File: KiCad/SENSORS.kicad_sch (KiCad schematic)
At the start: 10 parts, among them IC1 A3144EUA, J25 Screw_Terminal_01x02, U1 TMP102xxDRL

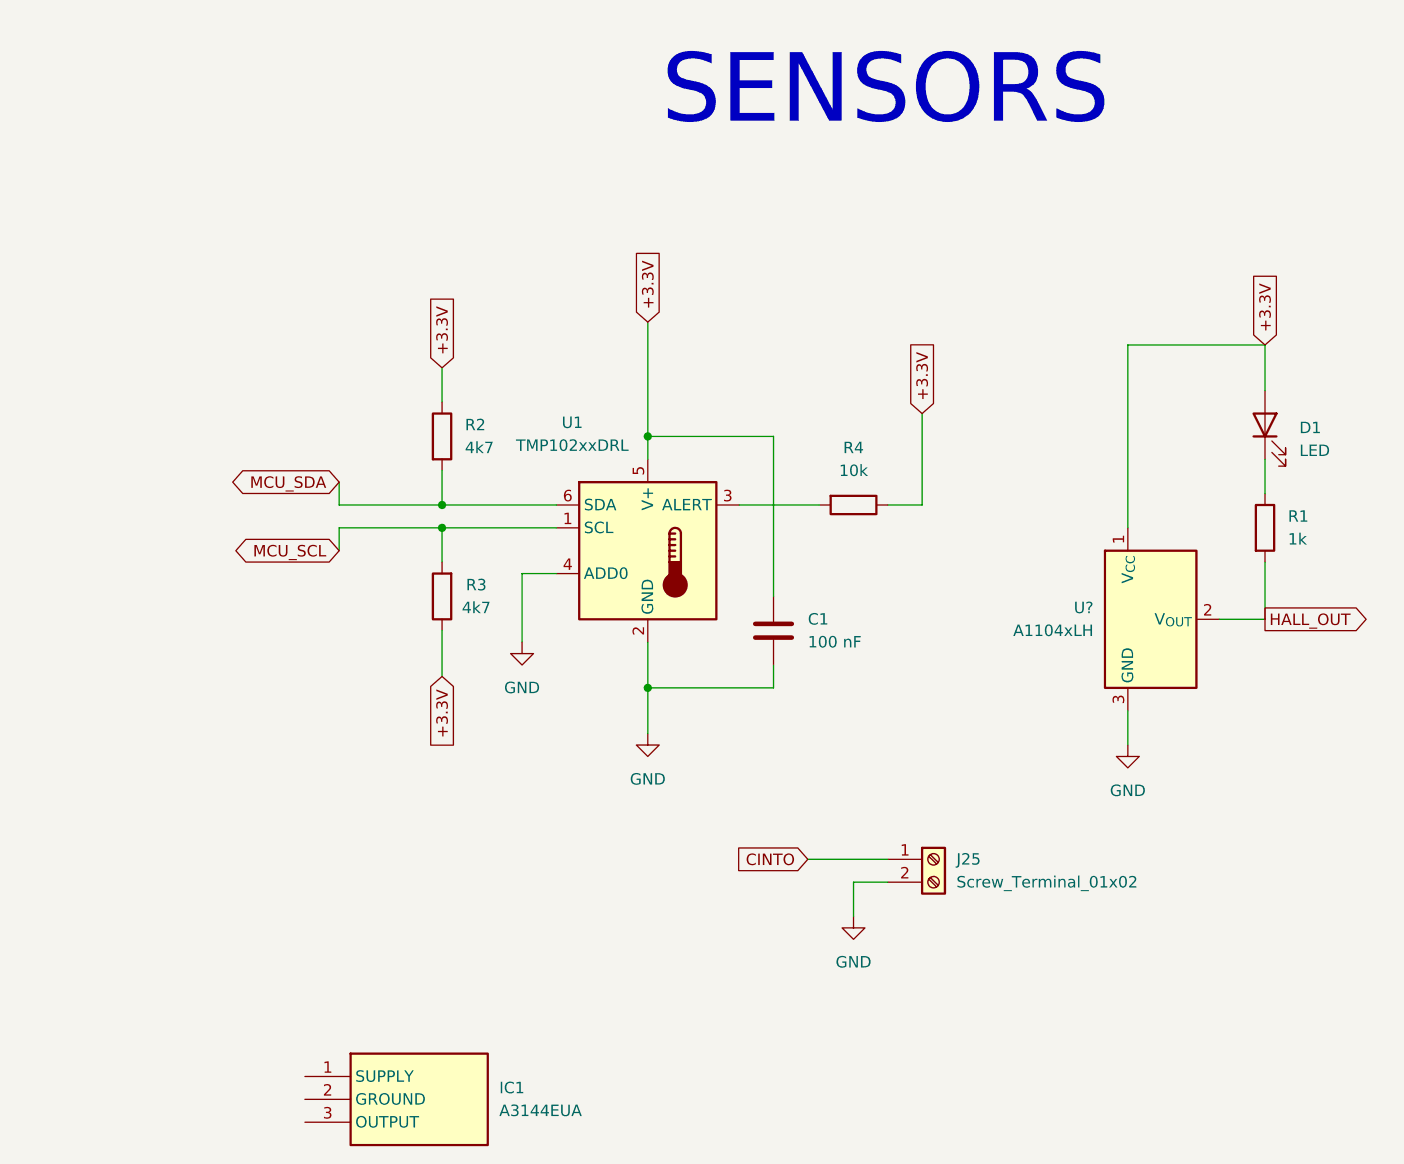
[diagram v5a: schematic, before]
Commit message: Modificació al HALL A3144
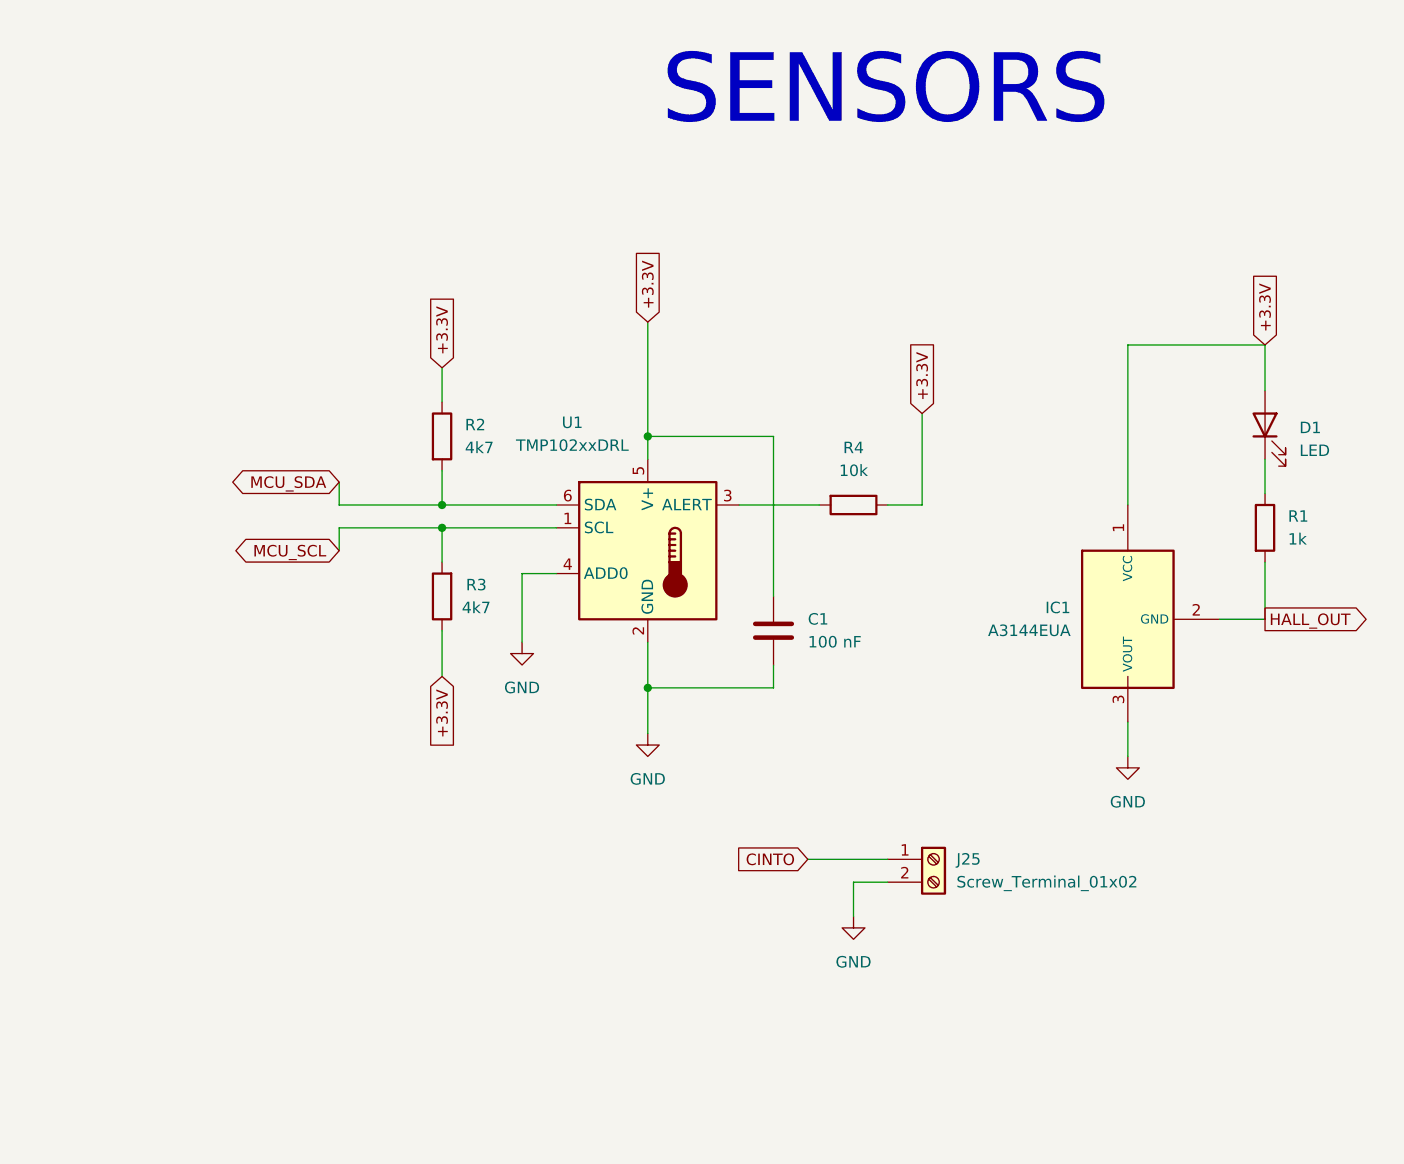
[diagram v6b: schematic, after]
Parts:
- removed U?: A1104xLH, Package_TO_SOT_SMD:SOT-23W, symbol Sensor_Magnetic:A1104xLH
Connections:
- net +3.3V: now also IC1.1 (VCC)
- net GND: now also IC1.3 (VOUT)
- net HALL_OUT: now also IC1.2 (GND)
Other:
- moved on the sheet: IC1
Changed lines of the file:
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@@
 	(wire
 		(pts
-			(xy 176.53 124.46) (xy 176.53 128.27)
+			(xy 176.53 125.73) (xy 176.53 129.54)
 		)
 		(stroke
@@
 	(wire
 		(pts
-			(xy 176.53 104.14) (xy 176.53 83.82)
+			(xy 176.53 101.6) (xy 176.53 83.82)
 		)
 		(stroke
@@
 	)
 	(symbol
-		(lib_name "A1104xLH_1")
-		(lib_id "Sensor_Magnetic:A1104xLH")
-		(at 179.07 114.3 0)
+		(lib_id "A3144:A3144EUA")
+		(at 166.37 110.49 0)
 		(unit 1)
 		(exclude_from_sim no)
@@
 		(dnp no)
 		(fields_autoplaced yes)
-		(property "Reference" "U?"
-			(at 172.72 113.0299 0)
+		(property "Reference" "IC1"
+			(at 170.18 113.0299 0)
 			(effects
 				(font
@@
 			)
 		)
-		(property "Value" "A1104xLH"
-			(at 172.72 115.5699 0)
+		(property "Value" "A3144EUA"
+			(at 170.18 115.5699 0)
 			(effects
 				(font
@@
 			)
 		)
-		(property "Footprint" "Package_TO_SOT_SMD:SOT-23W"
-			(at 179.07 131.572 0)
-			(effects
-				(font
-					(size 1.27 1.27)
-					(italic yes)
-				)
-				(hide yes)
-			)
-		)
-		(property "Datasheet" "https://www.allegromicro.com/-/media/files/datasheets/a110x-datasheet.ashx"
-			(at 179.07 127 0)
-			(effects
-				(font
-					(size 1.27 1.27)
-				)
-				(hide yes)
-			)
-		)
-		(property "Description" "Hall effect switch, unipolar (south-polarity), Bop=70-350G, Brp=50-330G, 3.8-24V supply, SOT-23W"
-			(at 179.07 129.286 0)
-			(effects
-				(font
-					(size 1.27 1.27)
-				)
-				(hide yes)
-			)
-		)
-		(pin "3"
-		)
-		(pin "2"
-		)
-		(pin "1"
-		)
-		(instances
-			(project "SENSORS"
-				(path "/264905d4-7c45-4183-babb-a5b2177ba886"
-					(reference "U?")
-					(unit 1)
-				)
-			)
-			(project ""
-				(path "/b6401b4f-5426-49b8-bb2e-8ecdb19989ef/e4bd2572-b2cc-4f8d-9ea8-3fa488d49274"
-					(reference "U9")
-					(unit 1)
-				)
-			)
-		)
-	)
-	(symbol
-		(lib_id "A3144:A3144EUA")
-		(at 85.09 165.1 0)
-		(unit 1)
-		(exclude_from_sim no)
-		(in_bom yes)
-		(on_board yes)
-		(dnp no)
-		(fields_autoplaced yes)
-		(property "Reference" "IC1"
-			(at 106.68 166.3699 0)
-			(effects
-				(font
-					(size 1.27 1.27)
-				)
-				(justify left)
-			)
-		)
-		(property "Value" "A3144EUA"
-			(at 106.68 168.9099 0)
-			(effects
-				(font
-					(size 1.27 1.27)
-				)
-				(justify left)
-			)
-		)
 		(property "Footprint" "A3144:A3144EUA"
-			(at 106.68 260.02 0)
+			(at 187.96 205.41 0)
 			(effects
 				(font
@@
 		)
 		(property "Datasheet" "https://pdf1.alldatasheet.com/datasheet-pdf/download/90853/ALLEGRO/A3144EUA.html"
-			(at 106.68 360.02 0)
+			(at 187.96 305.41 0)
 			(effects
 				(font
@@
 		)
 		(property "Description" "SENSITIVE HALL-EFFECT SWITCHES FOR HIGH-TEMPERATURE OPERATION"
-			(at 85.09 165.1 0)
+			(at 166.37 110.49 0)
 			(effects
 				(font
@@
 		)
 		(property "Height" "5.26"
-			(at 106.68 560.02 0)
+			(at 187.96 505.41 0)
 			(effects
 				(font
@@
 		)
 		(property "Manufacturer_Name" "Allegro Microsystems"
-			(at 106.68 660.02 0)
+			(at 187.96 605.41 0)
 			(effects
 				(font
@@
 		)
 		(property "Manufacturer_Part_Number" "A3144EUA"
-			(at 106.68 760.02 0)
+			(at 187.96 705.41 0)
 			(effects
 				(font
@@
 		)
 		(property "Mouser Part Number" ""
-			(at 106.68 860.02 0)
+			(at 187.96 805.41 0)
 			(effects
 				(font
@@
 		)
 		(property "Mouser Price/Stock" ""
-			(at 106.68 960.02 0)
+			(at 187.96 905.41 0)
 			(effects
 				(font
@@
 		)
 		(property "Arrow Part Number" ""
-			(at 106.68 1060.02 0)
+			(at 187.96 1005.41 0)
 			(effects
 				(font
@@
 		)
 		(property "Arrow Price/Stock" ""
-			(at 106.68 1160.02 0)
+			(at 187.96 1105.41 0)
 			(effects
 				(font
@@
 	(symbol
 		(lib_id "power:GND")
-		(at 176.53 128.27 0)
+		(at 176.53 129.54 0)
 		(unit 1)
 		(exclude_from_sim no)
@@
 		(fields_autoplaced yes)
 		(property "Reference" "#PWR03"
+			(at 176.53 135.89 0)
+			(effects
+				(font
+					(size 1.27 1.27)
+				)
+				(hide yes)
+			)
+		)
+		(property "Value" "GND"
 			(at 176.53 134.62 0)
 			(effects
@@
 					(size 1.27 1.27)
 				)
-				(hide yes)
-			)
-		)
-		(property "Value" "GND"
-			(at 176.53 133.35 0)
-			(effects
-				(font
-					(size 1.27 1.27)
-				)
 			)
 		)
 		(property "Footprint" ""
-			(at 176.53 128.27 0)
+			(at 176.53 129.54 0)
 			(effects
 				(font
@@
 		)
 		(property "Datasheet" ""
-			(at 176.53 128.27 0)
+			(at 176.53 129.54 0)
 			(effects
 				(font
@@
 		)
 		(property "Description" "Power symbol creates a global label with name \"GND\" , ground"
-			(at 176.53 128.27 0)
-			(effects
-				(font
+			(at 176.53 129.54 0)
+			(effects
+				(font

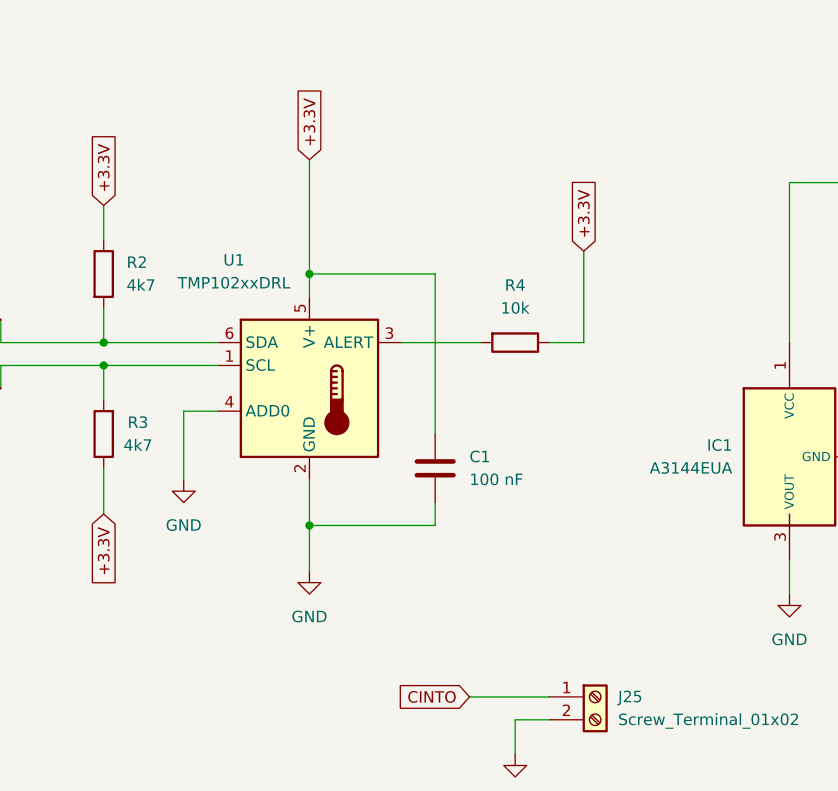
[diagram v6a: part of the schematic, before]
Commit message: Modificació als SENSORS
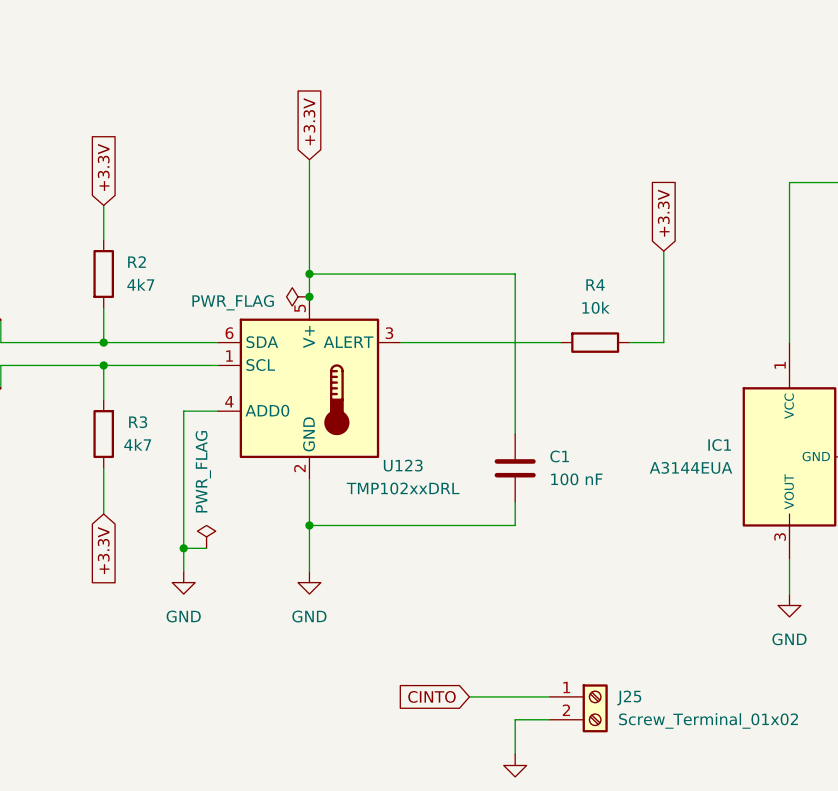
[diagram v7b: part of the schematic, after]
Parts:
- renumbered U1 to U123
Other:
- moved on the sheet: C1, R4
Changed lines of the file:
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@@
+	)
+	(junction
+		(at 109.22 124.46)
+		(diameter 0)
+		(color 0 0 0 0)
 	)
 	(junction
@@
 		(color 0 0 0 0)
 	)
+	(junction
+		(at 123.19 96.52)
+		(diameter 0)
+		(color 0 0 0 0)
+	)
 	(wire
 		(pts
@@
 	(wire
 		(pts
-			(xy 153.67 101.6) (xy 153.67 91.44)
+			(xy 162.56 101.6) (xy 162.56 91.44)
 		)
 		(stroke
@@
 	(wire
 		(pts
+			(xy 109.22 124.46) (xy 111.76 124.46)
+		)
+		(stroke
+			(width 0)
+			(type default)
+		)
+	)
+	(wire
+		(pts
 			(xy 88.9 104.14) (xy 88.9 106.68)
 		)
@@
 	(wire
 		(pts
-			(xy 137.16 93.98) (xy 123.19 93.98)
-		)
-		(stroke
-			(width 0)
-			(type default)
-		)
-	)
-	(wire
-		(pts
 			(xy 191.77 96.52) (xy 191.77 100.33)
 		)
@@
 	(wire
 		(pts
-			(xy 137.16 121.92) (xy 123.19 121.92)
+			(xy 123.19 121.92) (xy 146.05 121.92)
 		)
 		(stroke
@@
 	(wire
 		(pts
-			(xy 149.86 101.6) (xy 153.67 101.6)
+			(xy 158.75 101.6) (xy 162.56 101.6)
+		)
+		(stroke
+			(width 0)
+			(type default)
+		)
+	)
+	(wire
+		(pts
+			(xy 133.35 101.6) (xy 151.13 101.6)
 		)
 		(stroke
@@
 	(wire
 		(pts
-			(xy 133.35 101.6) (xy 142.24 101.6)
-		)
-		(stroke
-			(width 0)
-			(type default)
-		)
-	)
-	(wire
-		(pts
-			(xy 137.16 111.76) (xy 137.16 93.98)
-		)
-		(stroke
-			(width 0)
-			(type default)
-		)
-	)
-	(wire
-		(pts
-			(xy 109.22 109.22) (xy 109.22 116.84)
+			(xy 146.05 111.76) (xy 146.05 93.98)
+		)
+		(stroke
+			(width 0)
+			(type default)
+		)
+	)
+	(wire
+		(pts
+			(xy 123.19 93.98) (xy 146.05 93.98)
+		)
+		(stroke
+			(width 0)
+			(type default)
+		)
+	)
+	(wire
+		(pts
+			(xy 109.22 109.22) (xy 109.22 124.46)
 		)
 		(stroke
@@
 	(wire
 		(pts
-			(xy 137.16 119.38) (xy 137.16 121.92)
+			(xy 146.05 119.38) (xy 146.05 121.92)
 		)
 		(stroke
@@
 		(pts
 			(xy 191.77 83.82) (xy 191.77 88.9)
+		)
+		(stroke
+			(width 0)
+			(type default)
+		)
+	)
+	(wire
+		(pts
+			(xy 109.22 124.46) (xy 109.22 127)
 		)
 		(stroke
@@
 	(global_label "+3.3V"
 		(shape input)
-		(at 153.67 91.44 90)
+		(at 162.56 91.44 90)
 		(fields_autoplaced yes)
 		(effects
@@
 		)
 		(property "Intersheetrefs" "${INTERSHEET_REFS}"
-			(at 153.67 82.77 90)
+			(at 162.56 82.77 90)
 			(effects
 				(font
@@
 	(symbol
 		(lib_id "Device:C")
-		(at 137.16 115.57 0)
+		(at 146.05 115.57 0)
 		(unit 1)
 		(exclude_from_sim no)
@@
 		(fields_autoplaced yes)
 		(property "Reference" "C1"
-			(at 140.97 114.2999 0)
+			(at 149.86 114.2999 0)
 			(effects
 				(font
@@
 		)
 		(property "Value" "100 nF"
-			(at 140.97 116.8399 0)
+			(at 149.86 116.8399 0)
 			(effects
 				(font
@@
 		)
 		(property "Footprint" "Capacitor_SMD:C_0805_2012Metric"
-			(at 138.1252 119.38 0)
+			(at 147.0152 119.38 0)
 			(effects
 				(font
@@
 		)
 		(property "Datasheet" "~"
-			(at 137.16 115.57 0)
+			(at 146.05 115.57 0)
 			(effects
 				(font
@@
 		)
 		(property "Description" "Unpolarized capacitor"
-			(at 137.16 115.57 0)
+			(at 146.05 115.57 0)
 			(effects
 				(font
@@
 		(on_board yes)
 		(dnp no)
-		(property "Reference" "U1"
-			(at 114.808 92.456 0)
+		(property "Reference" "U123"
+			(at 133.604 115.316 0)
 			(effects
 				(font
@@
 		)
 		(property "Value" "TMP102xxDRL"
-			(at 114.808 94.996 0)
+			(at 133.604 117.856 0)
 			(effects
 				(font
@@
 			(project ""
 				(path "/264905d4-7c45-4183-babb-a5b2177ba886"
-					(reference "U1")
+					(reference "U123")
 					(unit 1)
 				)
@@
 	(symbol
 		(lib_id "power:GND")
-		(at 109.22 116.84 0)
+		(at 109.22 127 0)
 		(unit 1)
 		(exclude_from_sim no)
@@
 		(fields_autoplaced yes)
 		(property "Reference" "#PWR01"
-			(at 109.22 123.19 0)
+			(at 109.22 133.35 0)
 			(effects
 				(font
@@
 		)
 		(property "Value" "GND"
-			(at 109.22 121.92 0)
+			(at 109.22 132.08 0)
 			(effects
 				(font
@@
 		)
 		(property "Footprint" ""
-			(at 109.22 116.84 0)
+			(at 109.22 127 0)
 			(effects
 				(font
@@
 		)
 		(property "Datasheet" ""
-			(at 109.22 116.84 0)
+			(at 109.22 127 0)
 			(effects
 				(font
@@
 		)
 		(property "Description" "Power symbol creates a global label with name \"GND\" , ground"
-			(at 109.22 116.84 0)
+			(at 109.22 127 0)
 			(effects
 				(font
@@
 	)
 	(symbol
+		(lib_id "power:PWR_FLAG")
+		(at 123.19 96.52 90)
+		(unit 1)
+		(exclude_from_sim no)
+		(in_bom yes)
+		(on_board yes)
+		(dnp no)
+		(property "Reference" "#FLG01"
+			(at 121.285 96.52 0)
+			(effects
+				(font
+					(size 1.27 1.27)
+				)
+				(hide yes)
+			)
+		)
+		(property "Value" "PWR_FLAG"
+			(at 119.38 97.028 90)
+			(effects
+				(font
+					(size 1.27 1.27)
+				)
+				(justify left)
+			)
+		)
+		(property "Footprint" ""
+			(at 123.19 96.52 0)
+			(effects
+				(font
+					(size 1.27 1.27)
+				)
+				(hide yes)
+			)
+		)
+		(property "Datasheet" "~"
+			(at 123.19 96.52 0)
+			(effects
+				(font
+					(size 1.27 1.27)
+				)
+				(hide yes)
+			)
+		)
+		(property "Description" "Special symbol for telling ERC where power comes from"
+			(at 123.19 96.52 0)
+			(effects
+				(font
+					(size 1.27 1.27)
+				)
+				(hide yes)
+			)
+		)
+		(pin "1"
+		)
+		(instances
+			(project ""
+				(path "/264905d4-7c45-4183-babb-a5b2177ba886"
+					(reference "#FLG01")
+					(unit 1)
+				)
+			)
+		)
+	)
+	(symbol
 		(lib_id "power:GND")
 		(at 123.19 127 0)
@@
 				(path "/b6401b4f-5426-49b8-bb2e-8ecdb19989ef/e4bd2572-b2cc-4f8d-9ea8-3fa488d49274"
 					(reference "#PWR013")
+					(unit 1)
+				)
+			)
+		)
+	)
+	(symbol
+		(lib_id "power:PWR_FLAG")
+		(at 111.76 124.46 0)
+		(unit 1)
+		(exclude_from_sim no)
+		(in_bom yes)
+		(on_board yes)
+		(dnp no)
+		(property "Reference" "#FLG02"
+			(at 111.76 122.555 0)
+			(effects
+				(font
+					(size 1.27 1.27)
+				)
+				(hide yes)
+			)
+		)
+		(property "Value" "PWR_FLAG"
+			(at 111.252 120.65 90)
+			(effects
+				(font
+					(size 1.27 1.27)
+				)
+				(justify left)
+			)
+		)
+		(property "Footprint" ""
+			(at 111.76 124.46 0)
+			(effects
+				(font
+					(size 1.27 1.27)
+				)
+				(hide yes)
+			)
+		)
+		(property "Datasheet" "~"
+			(at 111.76 124.46 0)
+			(effects
+				(font
+					(size 1.27 1.27)
+				)
+				(hide yes)
+			)
+		)
+		(property "Description" "Special symbol for telling ERC where power comes from"
+			(at 111.76 124.46 0)
+			(effects
+				(font
+					(size 1.27 1.27)
+				)
+				(hide yes)
+			)
+		)
+		(pin "1"
+		)
+		(instances
+			(project "SENSORS"
+				(path "/264905d4-7c45-4183-babb-a5b2177ba886"
+					(reference "#FLG02")
 					(unit 1)
 				)
@@
 	(symbol
 		(lib_id "Device:R")
-		(at 146.05 101.6 270)
+		(at 154.94 101.6 270)
 		(unit 1)
 		(exclude_from_sim no)
@@
 		(fields_autoplaced yes)
 		(property "Reference" "R4"
-			(at 146.05 95.25 90)
+			(at 154.94 95.25 90)
 			(effects
 				(font
@@
 		)
 		(property "Value" "10k"
-			(at 146.05 97.79 90)
+			(at 154.94 97.79 90)
 			(effects
 				(font
@@
 		)
 		(property "Footprint" "Resistor_SMD:R_0805_2012Metric"
-			(at 146.05 99.822 90)
+			(at 154.94 99.822 90)
 			(effects
 				(font
@@
 		)
 		(property "Datasheet" "~"
-			(at 146.05 101.6 0)
+			(at 154.94 101.6 0)
 			(effects
 				(font
@@
 		)
 		(property "Description" "Resistor"
-			(at 146.05 101.6 0)
-			(effects
-				(font
+			(at 154.94 101.6 0)
+			(effects
+				(font
